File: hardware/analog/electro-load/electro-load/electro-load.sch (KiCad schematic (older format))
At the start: 30 parts, among them J1 AVR-ISP-10, SW1 RESET, U1 ATmega328P-AU, U10 ADS1115IDGS, U11 ADS1115IDGS, U2 MCP4725A0T-E_CH, U8 REF5040ID, U9 LMV321

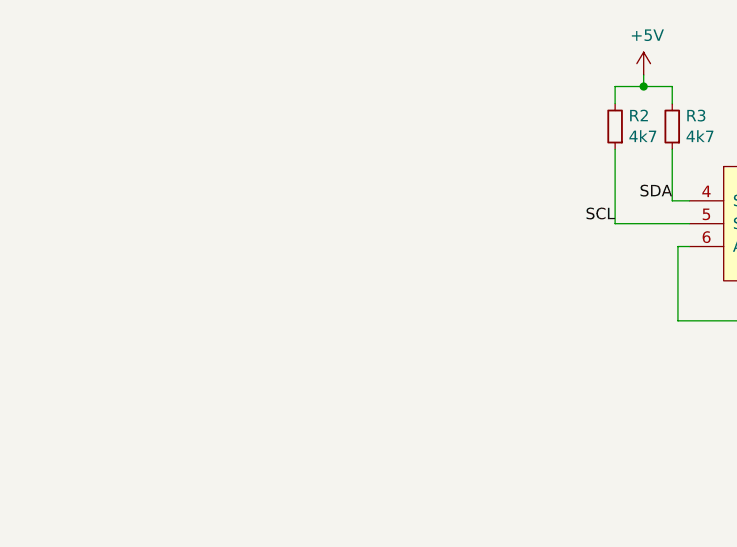
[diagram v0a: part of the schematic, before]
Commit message: Added mounting holes to schematic as well. Also made them solid ground anchors.
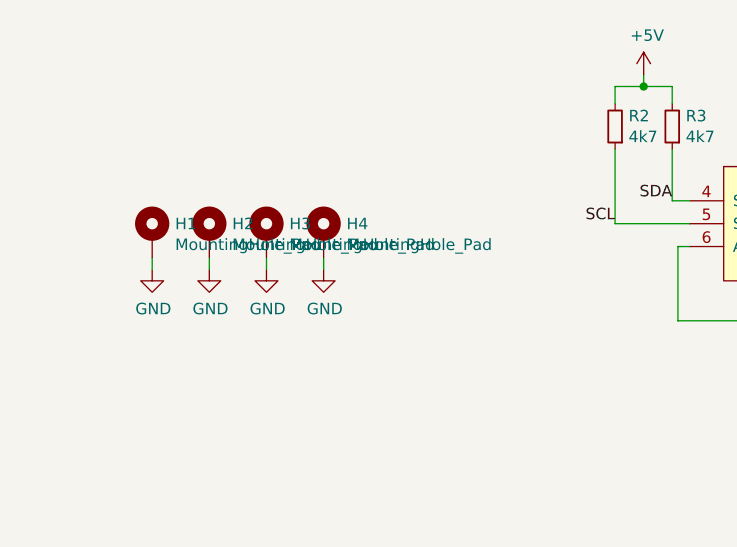
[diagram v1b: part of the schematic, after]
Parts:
- added H1, H2, H3, H4: MountingHole_Pad, MountingHole:MountingHole_3.2mm_M3_Pad_Via, symbol Mechanical:MountingHole_Pad
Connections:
- net GND: now also H1.1, H2.1, H3.1, H4.1
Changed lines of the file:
@@
 Wire Wire Line
 	1050 3875 1050 3775
+$Comp
+L Mechanical:MountingHole_Pad H1
+U 1 1 5EA4C4E2
+P 1125 1925
+F 0 "H1" H 1225 1974 50  0000 L CNN
+F 1 "MountingHole_Pad" H 1225 1883 50  0000 L CNN
+F 2 "MountingHole:MountingHole_3.2mm_M3_Pad_Via" H 1125 1925 50  0001 C CNN
+F 3 "~" H 1125 1925 50  0001 C CNN
+	1    1125 1925
+	1    0    0    -1
+$EndComp
+$Comp
+L power:GND #PWR0108
+U 1 1 5EA4CEE9
+P 1125 2075
+F 0 "#PWR0108" H 1125 1825 50  0001 C CNN
+F 1 "GND" H 1130 1902 50  0000 C CNN
+F 2 "" H 1125 2075 50  0001 C CNN
+F 3 "" H 1125 2075 50  0001 C CNN
+	1    1125 2075
+	1    0    0    -1
+$EndComp
+Wire Wire Line
+	1125 2075 1125 2025
+$Comp
+L Mechanical:MountingHole_Pad H2
+U 1 1 5EA58747
+P 1375 1925
+F 0 "H2" H 1475 1974 50  0000 L CNN
+F 1 "MountingHole_Pad" H 1475 1883 50  0000 L CNN
+F 2 "MountingHole:MountingHole_3.2mm_M3_Pad_Via" H 1375 1925 50  0001 C CNN
+F 3 "~" H 1375 1925 50  0001 C CNN
+	1    1375 1925
+	1    0    0    -1
+$EndComp
+$Comp
+L power:GND #PWR0109
+U 1 1 5EA58751
+P 1375 2075
+F 0 "#PWR0109" H 1375 1825 50  0001 C CNN
+F 1 "GND" H 1380 1902 50  0000 C CNN
+F 2 "" H 1375 2075 50  0001 C CNN
+F 3 "" H 1375 2075 50  0001 C CNN
+	1    1375 2075
+	1    0    0    -1
+$EndComp
+Wire Wire Line
+	1375 2075 1375 2025
+$Comp
+L Mechanical:MountingHole_Pad H3
+U 1 1 5EA5E1DB
+P 1625 1925
+F 0 "H3" H 1725 1974 50  0000 L CNN
+F 1 "MountingHole_Pad" H 1725 1883 50  0000 L CNN
+F 2 "MountingHole:MountingHole_3.2mm_M3_Pad_Via" H 1625 1925 50  0001 C CNN
+F 3 "~" H 1625 1925 50  0001 C CNN
+	1    1625 1925
+	1    0    0    -1
+$EndComp
+$Comp
+L power:GND #PWR0110
+U 1 1 5EA5E1E5
+P 1625 2075
+F 0 "#PWR0110" H 1625 1825 50  0001 C CNN
+F 1 "GND" H 1630 1902 50  0000 C CNN
+F 2 "" H 1625 2075 50  0001 C CNN
+F 3 "" H 1625 2075 50  0001 C CNN
+	1    1625 2075
+	1    0    0    -1
+$EndComp
+Wire Wire Line
+	1625 2075 1625 2025
+$Comp
+L Mechanical:MountingHole_Pad H4
+U 1 1 5EA5E1F0
+P 1875 1925
+F 0 "H4" H 1975 1974 50  0000 L CNN
+F 1 "MountingHole_Pad" H 1975 1883 50  0000 L CNN
+F 2 "MountingHole:MountingHole_3.2mm_M3_Pad_Via" H 1875 1925 50  0001 C CNN
+F 3 "~" H 1875 1925 50  0001 C CNN
+	1    1875 1925
+	1    0    0    -1
+$EndComp
+$Comp
+L power:GND #PWR0111
+U 1 1 5EA5E1FA
+P 1875 2075
+F 0 "#PWR0111" H 1875 1825 50  0001 C CNN
+F 1 "GND" H 1880 1902 50  0000 C CNN
+F 2 "" H 1875 2075 50  0001 C CNN
+F 3 "" H 1875 2075 50  0001 C CNN
+	1    1875 2075
+	1    0    0    -1
+$EndComp
+Wire Wire Line
+	1875 2075 1875 2025
 $EndSCHEMATC
